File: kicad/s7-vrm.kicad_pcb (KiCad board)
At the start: 2 copper layers, 61.7 x 53 mm, 36 parts, among them J1 Conn_02x15_Row_Letter_First, J2 Conn_02x02_Odd_Even, Q1 Q_NPN_BEC_BRT, Q2 Q_NMOS_GDS, Q3 Q_NMOS_GDS, Q4 Q_PNP_BEC_BRT, SW1 SW_DIP_x04, U1 ISL6545

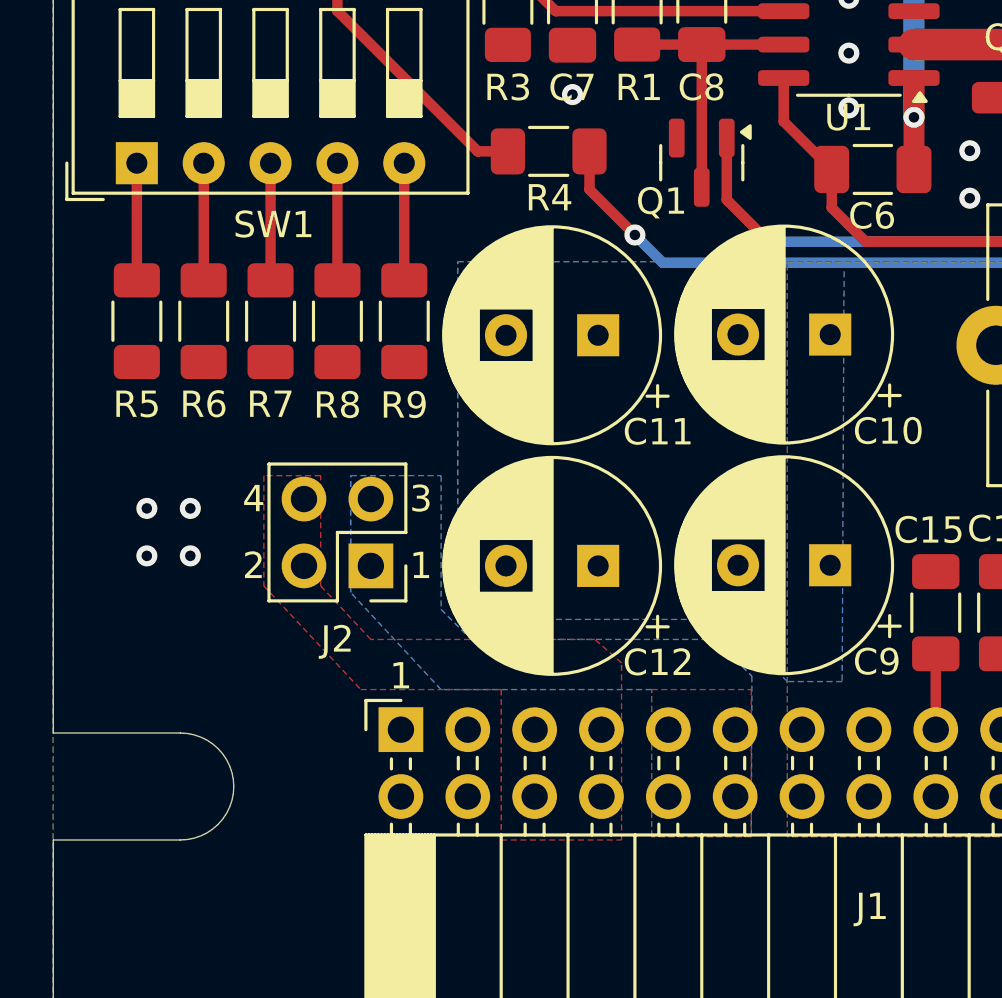
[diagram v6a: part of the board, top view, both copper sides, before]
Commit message: minor layout fixes
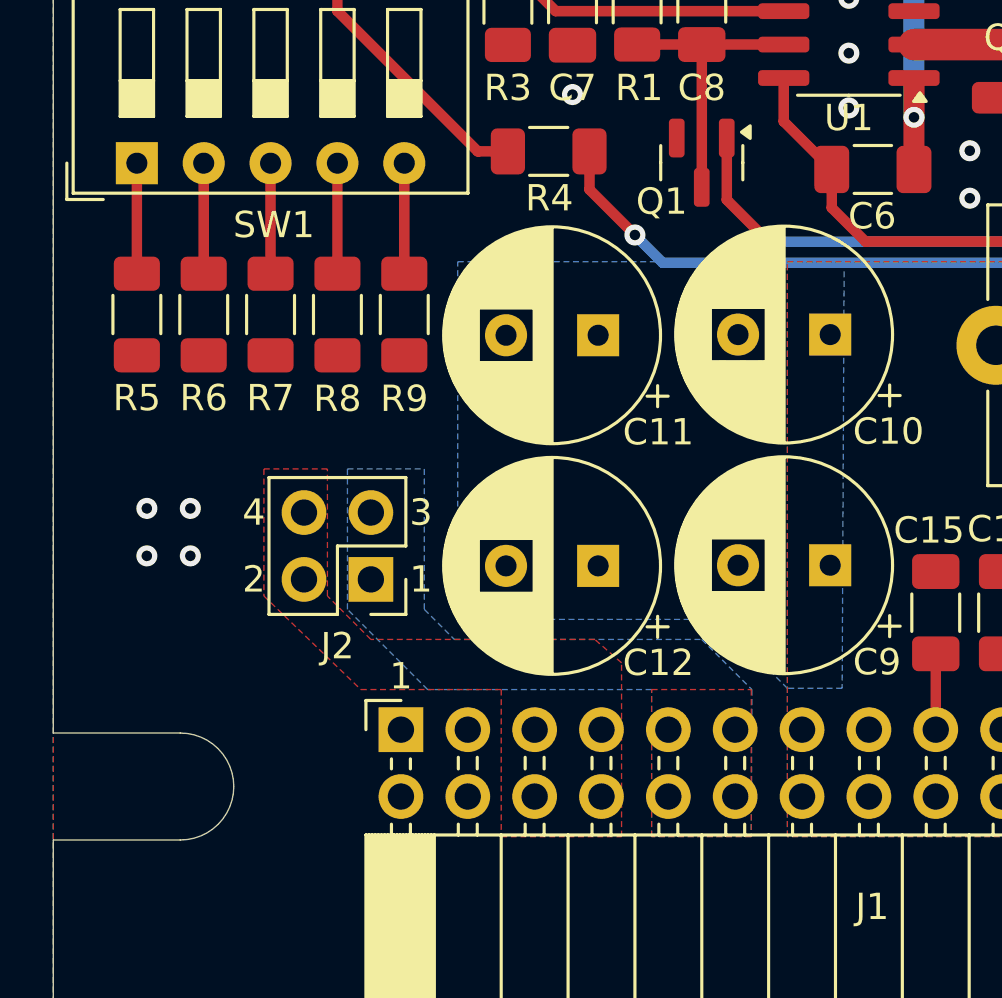
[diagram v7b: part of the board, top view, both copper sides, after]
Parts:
- removed the REF** at (127.4, 103.2)
- added REF**: OSHW-Logo2_14.6x12mm_SilkScreen, Symbol:OSHW-Logo2_14.6x12mm_SilkScreen, B.Cu at (158.8, 110.6)
- moved J2 0.51 mm to (131.2, 112.7)
- moved R5 0.25 mm to (122.3, 102.6)
- moved R6 0.25 mm to (124.8, 102.6)
- moved R7 0.25 mm to (127.4, 102.6)
- moved R8 0.25 mm to (129.9, 102.6)
- moved R9 0.25 mm to (132.5, 102.6)
